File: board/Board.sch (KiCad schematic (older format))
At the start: 59 parts, among them J1 GS3, J10 CONN_01X03, J11 CONN_01X03, J12 GS3, J13 GS3, J14 CONN_01X02, J15 CONN_01X03, J16 GS2, J17 CONN_01X01, J2 CONN_02X04, J3 CONN_01X03, J4 CONN_01X03, J5 CONN_01X03, J6 CONN_01X03, J7 CONN_01X03, J8 CONN_01X03, J9 CONN_01X03, SW1 SW_Push, U1 STM32F410RBTx, U2 SN74LVC1G04, U3 LF33ABDT-TR, U4 ICM-20689, U5 MAG3110, U6 MS5637, Y1 25 MHz

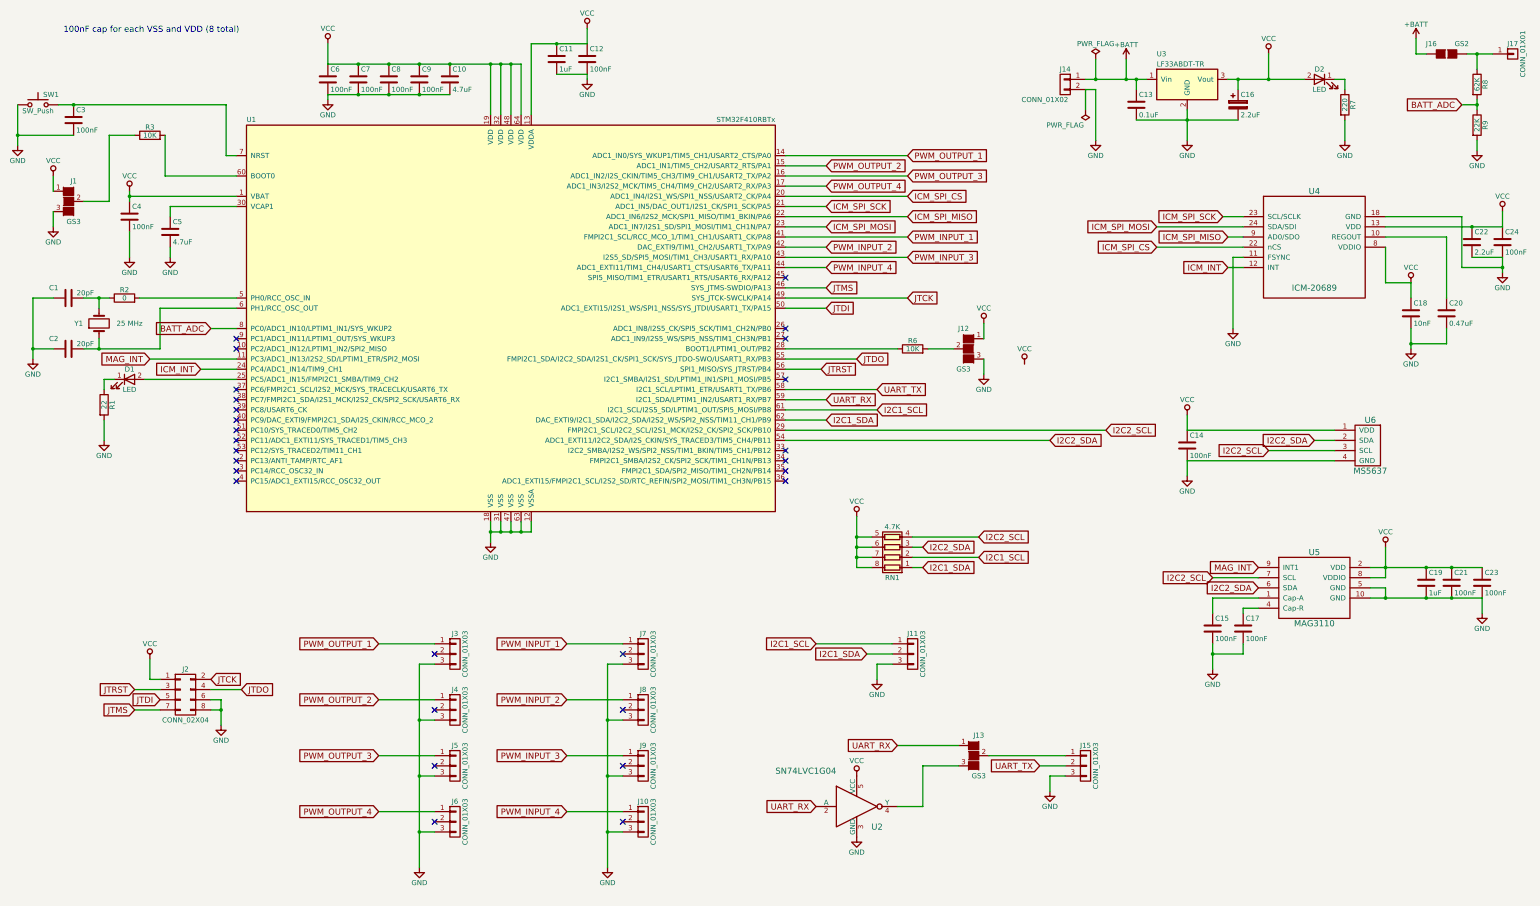
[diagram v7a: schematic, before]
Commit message: exposed another UART
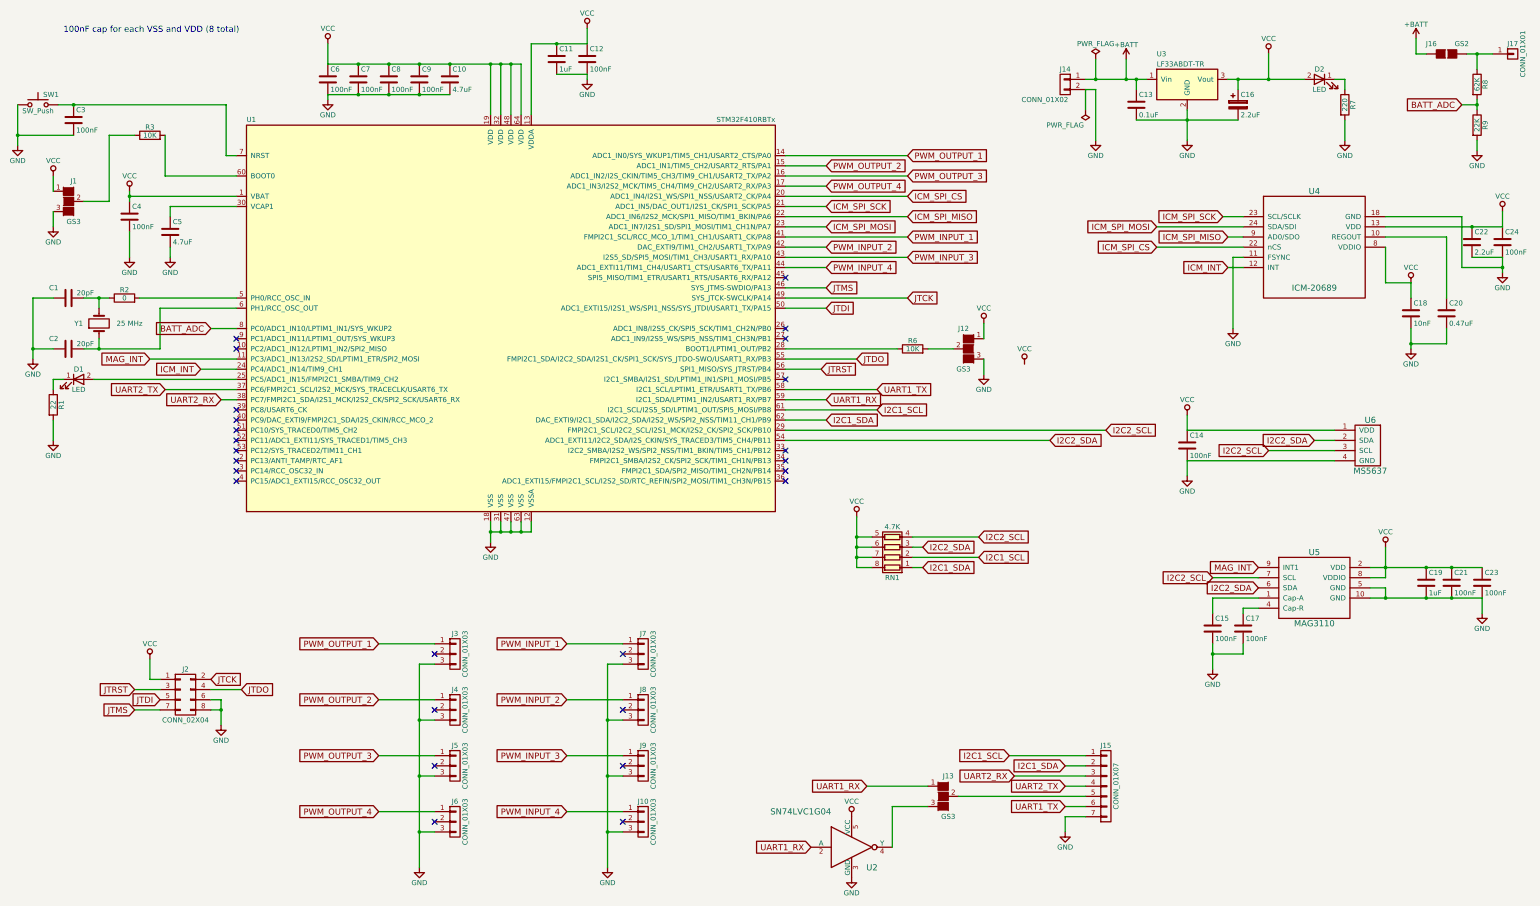
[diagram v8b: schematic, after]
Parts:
- removed J11, J15: CONN_01X03, Pin_Headers:Pin_Header_Straight_1x03_Pitch2.54mm, symbol CONN_01X03
- added J15: CONN_01X07, Pin_Headers:Pin_Header_Straight_1x07_Pitch2.54mm, symbol CONN_01X07
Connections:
- net GND: now also J15.7 (P7)
- net I2C1_SCL: now also J15.1 (P1)
- net I2C1_SDA: now also J15.2 (P2)
- net UART2_TX: now reaches U1.37 (PC6/FMPI2C1_SCL/I2S2_MCK/SYS_TRACECLK/USART6_TX)
- net UART2_TX: now also J15.4 (P4)
- net UART2_RX: now reaches U1.38 (PC7/FMPI2C1_SDA/I2S1_MCK/I2S2_CK/SPI2_SCK/USART6_RX)
- net UART2_RX: now also J15.3 (P3)
- net at J13.2 (G2): now also J15.5 (P5)
- net UART_RX renamed UART1_RX
- net UART_TX renamed UART1_TX
- net UART1_TX: now also J15.6 (P6)
- no-connect marks 28 -> 26
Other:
- moved on the sheet: D1, J13, R1, U2
